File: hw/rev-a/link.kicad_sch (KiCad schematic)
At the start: 26 parts, among them J10 TYPE-C-31-M-12, J11 Link cable, U10 USBLC6-2SC6, U11 SN74LVC1T45DBVR, U12 SN74LVC1T45DBVR, U13 SN74LVC1T45DBVR, U14 TPD4E05U06DQAR

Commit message: Schematic: renumber Link parts to 101+ (clashed with RPi core refs)
Co-Authored-By: Claude Opus 5.5 (1M context) <noreply@anthropic.com>
Claude-Session: https://claude.ai/code/session_01MZ3uQJCcn6FcjzVDhZnLJN
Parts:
- removed C10, C11, C12, C13, C14, C15: 100n, Capacitor_SMD:C_0402_1005Metric, symbol Device:C
- removed D10: green, LED_SMD:LED_0805_2012Metric, symbol Device:LED
- removed J10: TYPE-C-31-M-12, Connector_USB:USB_C_Receptacle_HRO_TYPE-C-31-M-12, symbol Connector:USB_C_Receptacle_USB2.0_16P
- removed J11: Link cable, Connector_Wire:SolderWire-0.15sqmm_1x05_P4mm_D0.5mm_OD1.5mm_Relief, symbol Connector_Generic:Conn_01x05
- removed R10, R11: 5.1k, Resistor_SMD:R_0402_1005Metric, symbol Device:R
- removed R12, R16, R17: 100k, Resistor_SMD:R_0402_1005Metric, symbol Device:R
- removed R13, R14, R15: 33, Resistor_SMD:R_0402_1005Metric, symbol Device:R
- removed R18: 100, Resistor_SMD:R_0402_1005Metric, symbol Device:R
- removed TP10: SWCLK, TestPoint:TestPoint_Pad_D1.0mm, symbol Connector:TestPoint
- removed TP11: SWD, TestPoint:TestPoint_Pad_D1.0mm, symbol Connector:TestPoint
- removed TP12: GND, TestPoint:TestPoint_Pad_D1.0mm, symbol Connector:TestPoint
- removed U10: USBLC6-2SC6, Package_TO_SOT_SMD:SOT-23-6, symbol Power_Protection:USBLC6-2SC6
- removed U11, U12, U13: SN74LVC1T45DBVR, Package_TO_SOT_SMD:SOT-23-6, symbol Logic_LevelTranslator:SN74LVC1T45DBV
- removed U14: TPD4E05U06DQAR, Package_SON:USON-10_2.5x1.0mm_P0.5mm, symbol Power_Protection:TPD4E05U06DQA
- added C101, C102, C103, C104, C105, C106: 100n, Capacitor_SMD:C_0402_1005Metric, symbol Device:C
- added D101: green, LED_SMD:LED_0805_2012Metric, symbol Device:LED
- added J101: TYPE-C-31-M-12, Connector_USB:USB_C_Receptacle_HRO_TYPE-C-31-M-12, symbol Connector:USB_C_Receptacle_USB2.0_16P
- added J102: Link cable, Connector_Wire:SolderWire-0.15sqmm_1x05_P4mm_D0.5mm_OD1.5mm_Relief, symbol Connector_Generic:Conn_01x05
- added R101, R102: 5.1k, Resistor_SMD:R_0402_1005Metric, symbol Device:R
- added R103, R107, R108: 100k, Resistor_SMD:R_0402_1005Metric, symbol Device:R
- added R104, R105, R106: 33, Resistor_SMD:R_0402_1005Metric, symbol Device:R
- added R109: 100, Resistor_SMD:R_0402_1005Metric, symbol Device:R
- added TP101: SWCLK, TestPoint:TestPoint_Pad_D1.0mm, symbol Connector:TestPoint
- added TP102: SWD, TestPoint:TestPoint_Pad_D1.0mm, symbol Connector:TestPoint
- added TP103: GND, TestPoint:TestPoint_Pad_D1.0mm, symbol Connector:TestPoint
- added U101: USBLC6-2SC6, Package_TO_SOT_SMD:SOT-23-6, symbol Power_Protection:USBLC6-2SC6
- added U102, U103, U104: SN74LVC1T45DBVR, Package_TO_SOT_SMD:SOT-23-6, symbol Logic_LevelTranslator:SN74LVC1T45DBV
- added U105: TPD4E05U06DQAR, Package_SON:USON-10_2.5x1.0mm_P0.5mm, symbol Power_Protection:TPD4E05U06DQA
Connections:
- net +3V3: now also C101.1, C103.1, C105.1, U102.1 (VCCA), U103.1 (VCCA), U104.1 (VCCA), U104.5 (DIR)
- net B_SCK: now also R104.1, U102.4 (B)
- net B_SI: now also R106.1, U104.4 (B)
- net B_SO: now also R105.1, U103.4 (B)
- net CC1: now also J101.A5 (CC1), R101.1
- net CC2: now also J101.B5 (CC2), R102.1
- net GND: now also C101.2, C102.2, C103.2, C104.2, C105.2, C106.2, D101.1 (K), J101.A1 (GND), J101.A12 (GND), J101.B1 (GND), J101.B12 (GND), J101.SH (SHIELD), J102.1 (Pin_1), J102.3 (Pin_3), R101.2, R102.2, R103.2, TP103.1, U101.2 (GND), U102.2 (GND), U103.2 (GND), U103.5 (DIR), U104.2 (GND), U105.3 (GND), U105.8 (GND)
- net GPIO0: now also U102.3 (A)
- net GPIO1: now also U103.3 (A)
- net GPIO2: now also U104.3 (A)
- net GPIO25: now also R109.1
- net GPIO3: now also R103.1, U102.5 (DIR)
- net LED_A: now also D101.2 (A), R109.2
- net LINK_SCK: now also J102.2 (Pin_2), R104.2, R107.2, U105.1 (D1+)
- net LINK_SI: now also J102.5 (Pin_5), R106.2, U105.4 (D2+)
- net LINK_SO: now also J102.4 (Pin_4), R105.2, R108.2, U105.2 (D1-)
- net SWCLK: now also TP101.1
- net SWD: now also TP102.1
- net USB_D+: now also J101.A6 (D+), J101.B6 (D+), U101.3 (I/O2), U101.4 (I/O2)
- net USB_D-: now also J101.A7 (D-), J101.B7 (D-), U101.1 (I/O1), U101.6 (I/O1)
- net VBUS: now also C102.1, C104.1, C106.1, J101.A4 (VBUS), J101.A9 (VBUS), J101.B4 (VBUS), J101.B9 (VBUS), R107.1, R108.1, U101.5 (VBUS), U102.6 (VCCB), U103.6 (VCCB), U104.6 (VCCB)
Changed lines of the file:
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@@
 		(on_board yes)
 		(dnp no)
-		(property "Reference" "J10"
+		(property "Reference" "J101"
 			(at 25.4 46.42 0)
 			(effects
@@
 			(project "gb-link-usb"
 				(path "/94683f5c-9cd9-448e-be96-9792537b5cb8/7d2e4b91-3c5a-4e8f-b6d0-9a1c2e3f4b58"
-					(reference "J10")
+					(reference "J101")
 					(unit 1)
 				)
@@
 		(on_board yes)
 		(dnp no)
-		(property "Reference" "R10"
+		(property "Reference" "R101"
 			(at 88.9 33.72 0)
 			(effects
@@
 			(project "gb-link-usb"
 				(path "/94683f5c-9cd9-448e-be96-9792537b5cb8/7d2e4b91-3c5a-4e8f-b6d0-9a1c2e3f4b58"
-					(reference "R10")
+					(reference "R101")
 					(unit 1)
 				)
@@
 		(on_board yes)
 		(dnp no)
-		(property "Reference" "R11"
+		(property "Reference" "R102"
 			(at 152.4 33.72 0)
 			(effects
@@
 			(project "gb-link-usb"
 				(path "/94683f5c-9cd9-448e-be96-9792537b5cb8/7d2e4b91-3c5a-4e8f-b6d0-9a1c2e3f4b58"
-					(reference "R11")
+					(reference "R102")
 					(unit 1)
 				)
@@
 		(on_board yes)
 		(dnp no)
-		(property "Reference" "U10"
+		(property "Reference" "U101"
 			(at 215.9 36.26 0)
 			(effects
@@
 			(project "gb-link-usb"
 				(path "/94683f5c-9cd9-448e-be96-9792537b5cb8/7d2e4b91-3c5a-4e8f-b6d0-9a1c2e3f4b58"
-					(reference "U10")
+					(reference "U101")
 					(unit 1)
 				)
@@
 		(on_board yes)
 		(dnp no)
-		(property "Reference" "U11"
+		(property "Reference" "U102"
 			(at 279.4 41.34 0)
 			(effects
@@
 			(project "gb-link-usb"
 				(path "/94683f5c-9cd9-448e-be96-9792537b5cb8/7d2e4b91-3c5a-4e8f-b6d0-9a1c2e3f4b58"
-					(reference "U11")
+					(reference "U102")
 					(unit 1)
 				)
@@
 		(on_board yes)
 		(dnp no)
-		(property "Reference" "R12"
+		(property "Reference" "R103"
 			(at 342.9 33.72 0)
 			(effects
@@
 			(project "gb-link-usb"
 				(path "/94683f5c-9cd9-448e-be96-9792537b5cb8/7d2e4b91-3c5a-4e8f-b6d0-9a1c2e3f4b58"
-					(reference "R12")
+					(reference "R103")
 					(unit 1)
 				)
@@
 		(on_board yes)
 		(dnp no)
-		(property "Reference" "U12"
+		(property "Reference" "U103"
 			(at 25.4 109.92 0)
 			(effects
@@
 			(project "gb-link-usb"
 				(path "/94683f5c-9cd9-448e-be96-9792537b5cb8/7d2e4b91-3c5a-4e8f-b6d0-9a1c2e3f4b58"
-					(reference "U12")
+					(reference "U103")
 					(unit 1)
 				)
@@
 		(on_board yes)
 		(dnp no)
-		(property "Reference" "U13"
+		(property "Reference" "U104"
 			(at 88.9 109.92 0)
 			(effects
@@
 			(project "gb-link-usb"
 				(path "/94683f5c-9cd9-448e-be96-9792537b5cb8/7d2e4b91-3c5a-4e8f-b6d0-9a1c2e3f4b58"
-					(reference "U13")
+					(reference "U104")
 					(unit 1)
 				)
@@
 		(on_board yes)
 		(dnp no)
-		(property "Reference" "C10"
+		(property "Reference" "C101"
 			(at 152.4 104.84 0)
 			(effects
@@
 			(project "gb-link-usb"
 				(path "/94683f5c-9cd9-448e-be96-9792537b5cb8/7d2e4b91-3c5a-4e8f-b6d0-9a1c2e3f4b58"
-					(reference "C10")
+					(reference "C101")
 					(unit 1)
 				)
@@
 		(on_board yes)
 		(dnp no)
-		(property "Reference" "C11"
+		(property "Reference" "C102"
 			(at 215.9 104.84 0)
 			(effects
@@
 			(project "gb-link-usb"
 				(path "/94683f5c-9cd9-448e-be96-9792537b5cb8/7d2e4b91-3c5a-4e8f-b6d0-9a1c2e3f4b58"
-					(reference "C11")
+					(reference "C102")
 					(unit 1)
 				)
@@
 		(on_board yes)
 		(dnp no)
-		(property "Reference" "C12"
+		(property "Reference" "C103"
 			(at 279.4 104.84 0)
 			(effects
@@
 			(project "gb-link-usb"
 				(path "/94683f5c-9cd9-448e-be96-9792537b5cb8/7d2e4b91-3c5a-4e8f-b6d0-9a1c2e3f4b58"
-					(reference "C12")
+					(reference "C103")
 					(unit 1)
 				)
@@
 		(on_board yes)
 		(dnp no)
-		(property "Reference" "C13"
+		(property "Reference" "C104"
 			(at 342.9 104.84 0)
 			(effects
@@
 			(project "gb-link-usb"
 				(path "/94683f5c-9cd9-448e-be96-9792537b5cb8/7d2e4b91-3c5a-4e8f-b6d0-9a1c2e3f4b58"
-					(reference "C13")
+					(reference "C104")
 					(unit 1)
 				)
@@
 		(on_board yes)
 		(dnp no)
-		(property "Reference" "C14"
+		(property "Reference" "C105"
 			(at 25.4 155.64 0)
 			(effects
@@
 			(project "gb-link-usb"
 				(path "/94683f5c-9cd9-448e-be96-9792537b5cb8/7d2e4b91-3c5a-4e8f-b6d0-9a1c2e3f4b58"
-					(reference "C14")
+					(reference "C105")
 					(unit 1)
 				)
@@
 		(on_board yes)
 		(dnp no)
-		(property "Reference" "C15"
+		(property "Reference" "C106"
 			(at 88.9 155.64 0)
 			(effects
@@
 			(project "gb-link-usb"
 				(path "/94683f5c-9cd9-448e-be96-9792537b5cb8/7d2e4b91-3c5a-4e8f-b6d0-9a1c2e3f4b58"
-					(reference "C15")
+					(reference "C106")
 					(unit 1)
 				)
@@
 		(on_board yes)
 		(dnp no)
-		(property "Reference" "R13"
+		(property "Reference" "R104"
 			(at 152.4 155.64 0)
 			(effects
@@
 			(project "gb-link-usb"
 				(path "/94683f5c-9cd9-448e-be96-9792537b5cb8/7d2e4b91-3c5a-4e8f-b6d0-9a1c2e3f4b58"
-					(reference "R13")
+					(reference "R104")
 					(unit 1)
 				)
@@
 		(on_board yes)
 		(dnp no)
-		(property "Reference" "R14"
+		(property "Reference" "R105"
 			(at 215.9 155.64 0)
 			(effects
@@
 			(project "gb-link-usb"
 				(path "/94683f5c-9cd9-448e-be96-9792537b5cb8/7d2e4b91-3c5a-4e8f-b6d0-9a1c2e3f4b58"
-					(reference "R14")
+					(reference "R105")
 					(unit 1)
 				)
@@
 		(on_board yes)
 		(dnp no)
-		(property "Reference" "R15"
+		(property "Reference" "R106"
 			(at 279.4 155.64 0)
 			(effects
@@
 			(project "gb-link-usb"
 				(path "/94683f5c-9cd9-448e-be96-9792537b5cb8/7d2e4b91-3c5a-4e8f-b6d0-9a1c2e3f4b58"
-					(reference "R15")
+					(reference "R106")
 					(unit 1)
 				)
@@
 		(on_board yes)
 		(dnp no)
-		(property "Reference" "R16"
+		(property "Reference" "R107"
 			(at 342.9 155.64 0)
 			(effects
@@
 			(project "gb-link-usb"
 				(path "/94683f5c-9cd9-448e-be96-9792537b5cb8/7d2e4b91-3c5a-4e8f-b6d0-9a1c2e3f4b58"
-					(reference "R16")
+					(reference "R107")
 					(unit 1)
 				)
@@
 		(on_board yes)
 		(dnp no)
-		(property "Reference" "R17"
+		(property "Reference" "R108"
 			(at 25.4 191.2 0)
 			(effects
@@
 			(project "gb-link-usb"
 				(path "/94683f5c-9cd9-448e-be96-9792537b5cb8/7d2e4b91-3c5a-4e8f-b6d0-9a1c2e3f4b58"
-					(reference "R17")
+					(reference "R108")
 					(unit 1)
 				)
@@
 		(on_board yes)
 		(dnp no)
-		(property "Reference" "U14"
+		(property "Reference" "U105"
 			(at 88.9 196.28 0)
 			(effects
@@
 			(project "gb-link-usb"
 				(path "/94683f5c-9cd9-448e-be96-9792537b5cb8/7d2e4b91-3c5a-4e8f-b6d0-9a1c2e3f4b58"
-					(reference "U14")
+					(reference "U105")
 					(unit 1)
 				)
@@
 		(on_board yes)
 		(dnp no)
-		(property "Reference" "J11"
+		(property "Reference" "J102"
 			(at 152.4 193.74 0)
 			(effects
@@
 			(project "gb-link-usb"
 				(path "/94683f5c-9cd9-448e-be96-9792537b5cb8/7d2e4b91-3c5a-4e8f-b6d0-9a1c2e3f4b58"
-					(reference "J11")
+					(reference "J102")
 					(unit 1)
 				)
@@
 		(on_board yes)
 		(dnp no)
-		(property "Reference" "D10"
+		(property "Reference" "D101"
 			(at 215.9 188.66 0)
 			(effects
@@
 			(project "gb-link-usb"
 				(path "/94683f5c-9cd9-448e-be96-9792537b5cb8/7d2e4b91-3c5a-4e8f-b6d0-9a1c2e3f4b58"
-					(reference "D10")
+					(reference "D101")
 					(unit 1)
 				)
@@
 		(on_board yes)
 		(dnp no)
-		(property "Reference" "R18"
+		(property "Reference" "R109"
 			(at 279.4 191.2 0)
 			(effects
@@
 			(project "gb-link-usb"
 				(path "/94683f5c-9cd9-448e-be96-9792537b5cb8/7d2e4b91-3c5a-4e8f-b6d0-9a1c2e3f4b58"
-					(reference "R18")
+					(reference "R109")
 					(unit 1)
 				)
@@
 		(on_board yes)
 		(dnp no)
-		(property "Reference" "TP10"
+		(property "Reference" "TP101"
 			(at 342.9 188.66 0)
 			(effects
@@
 			(project "gb-link-usb"
 				(path "/94683f5c-9cd9-448e-be96-9792537b5cb8/7d2e4b91-3c5a-4e8f-b6d0-9a1c2e3f4b58"
-					(reference "TP10")
+					(reference "TP101")
 					(unit 1)
 				)
@@
 		(on_board yes)
 		(dnp no)
-		(property "Reference" "TP11"
+		(property "Reference" "TP102"
 			(at 25.4 239.46 0)
 			(effects
@@
 			(project "gb-link-usb"
 				(path "/94683f5c-9cd9-448e-be96-9792537b5cb8/7d2e4b91-3c5a-4e8f-b6d0-9a1c2e3f4b58"
-					(reference "TP11")
+					(reference "TP102")
 					(unit 1)
 				)
@@
 		(on_board yes)
 		(dnp no)
-		(property "Reference" "TP12"
+		(property "Reference" "TP103"
 			(at 88.9 239.46 0)
 			(effects
@@
 			(project "gb-link-usb"
 				(path "/94683f5c-9cd9-448e-be96-9792537b5cb8/7d2e4b91-3c5a-4e8f-b6d0-9a1c2e3f4b58"
-					(reference "TP12")
+					(reference "TP103")
 					(unit 1)
 				)

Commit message: PCB rev A routed: scripted build + Freerouting pipeline, DRC 0 errors
Co-Authored-By: Claude Opus 5.5 (1M context) <noreply@anthropic.com>
Claude-Session: https://claude.ai/code/session_01MZ3uQJCcn6FcjzVDhZnLJN
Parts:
- removed TP101: SWCLK, TestPoint:TestPoint_Pad_D1.0mm, symbol Connector:TestPoint
- removed TP102: SWD, TestPoint:TestPoint_Pad_D1.0mm, symbol Connector:TestPoint
- removed TP103: GND, TestPoint:TestPoint_Pad_D1.0mm, symbol Connector:TestPoint
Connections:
- net GPIO0 renamed GPIO12
- net GPIO1 renamed GPIO13
- net GPIO2 renamed GPIO14
- net GPIO25 renamed GPIO21
- net GPIO3 renamed GPIO11

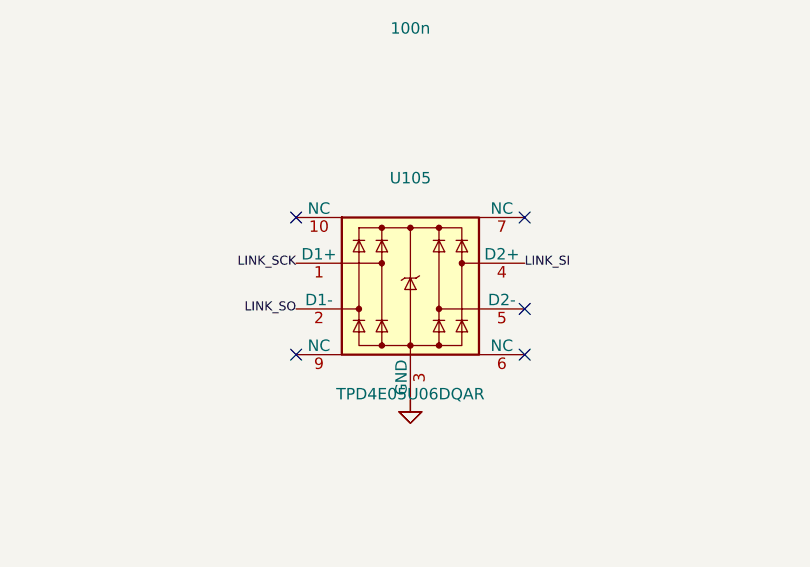
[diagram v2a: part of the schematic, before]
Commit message: PCB rev A: DRC 0 errors/0 unconnected, silk cleaned, local RPi libs
- TPD4E05U06 NC pins tied for straight-through routing (TI pin table)
- bottom GND pour runs to the board edge (sealed island fix)
- pcb_route retries Freerouting until DRC is clean
- LCSC fields off silk, designators on fab, pad labels
- extract_libs.py: RPi symbols/footprints + lib tables in the project
- renders in hw/rev-a/img

Co-Authored-By: Claude Opus 5.5 (1M context) <noreply@anthropic.com>
Claude-Session: https://claude.ai/code/session_01MZ3uQJCcn6FcjzVDhZnLJN
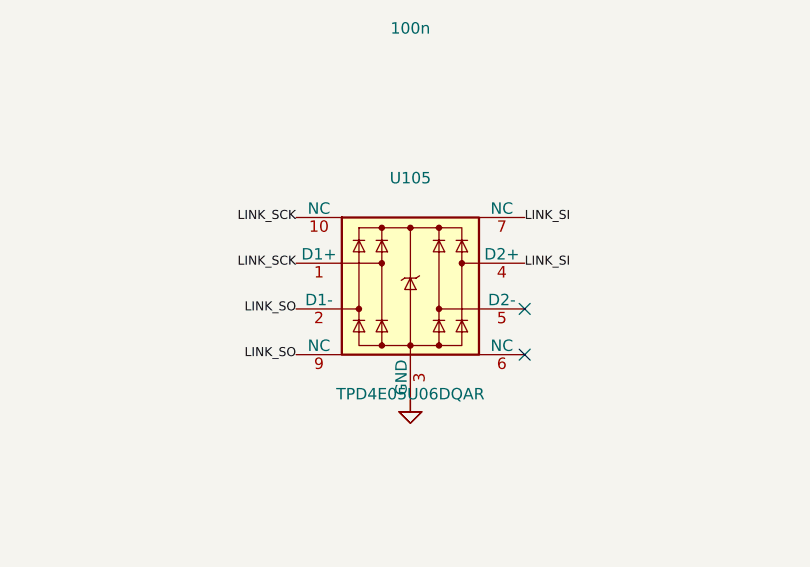
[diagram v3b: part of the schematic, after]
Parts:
- J102: now left out of the parts list
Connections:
- net LINK_SCK: now also U105.10 (NC)
- net LINK_SI: now also U105.7 (NC)
- net LINK_SO: now also U105.9 (NC)
- no-connect marks 7 -> 4
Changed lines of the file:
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@@
 		(at 101.6 215.9)
 	)
-	(no_connect
-		(at 101.6 200.66)
-	)
-	(no_connect
-		(at 76.2 215.9)
-	)
-	(no_connect
-		(at 76.2 200.66)
+	(label "LINK_SI"
+		(at 101.6 200.66 0)
+		(fields_autoplaced yes)
+		(effects
+			(font
+				(size 1.0 1.0)
+			)
+			(justify left)
+		)
+	)
+	(label "LINK_SO"
+		(at 76.2 215.9 180)
+		(fields_autoplaced yes)
+		(effects
+			(font
+				(size 1.0 1.0)
+			)
+			(justify right)
+		)
+	)
+	(label "LINK_SCK"
+		(at 76.2 200.66 180)
+		(fields_autoplaced yes)
+		(effects
+			(font
+				(size 1.0 1.0)
+			)
+			(justify right)
+		)
 	)
 	(symbol
@@
 		(unit 1)
 		(exclude_from_sim no)
-		(in_bom yes)
-		(on_board yes)
-		(dnp no)
+		(in_bom no)
+		(on_board yes)
+		(dnp no)
